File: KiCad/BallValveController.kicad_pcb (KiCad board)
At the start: 2 copper layers, 55.6 x 43.2 mm, 62 parts, among them J1 Screw_Terminal_01x03, J2 Screw_Terminal_01x04, J3 Screw_Terminal_01x04, J4 Screw_Terminal_01x04, J5 Conn_01x01_Male, J6 Screw_Terminal_01x04, J7 Screw_Terminal_01x02, K1 G5V-2, Q1 Q_PMOS_GDS, Q2 2N2222A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

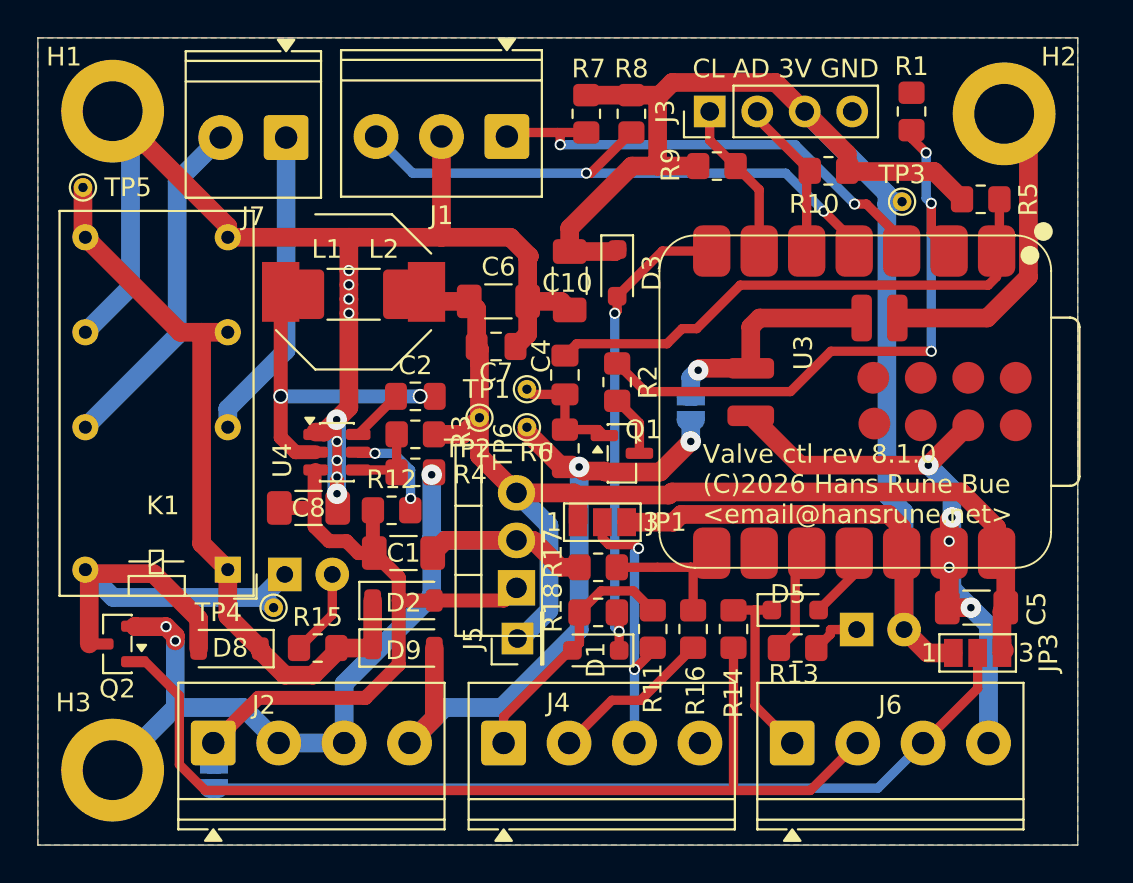
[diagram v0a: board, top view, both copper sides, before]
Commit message: Add ME3116 support via 1x3 pin header
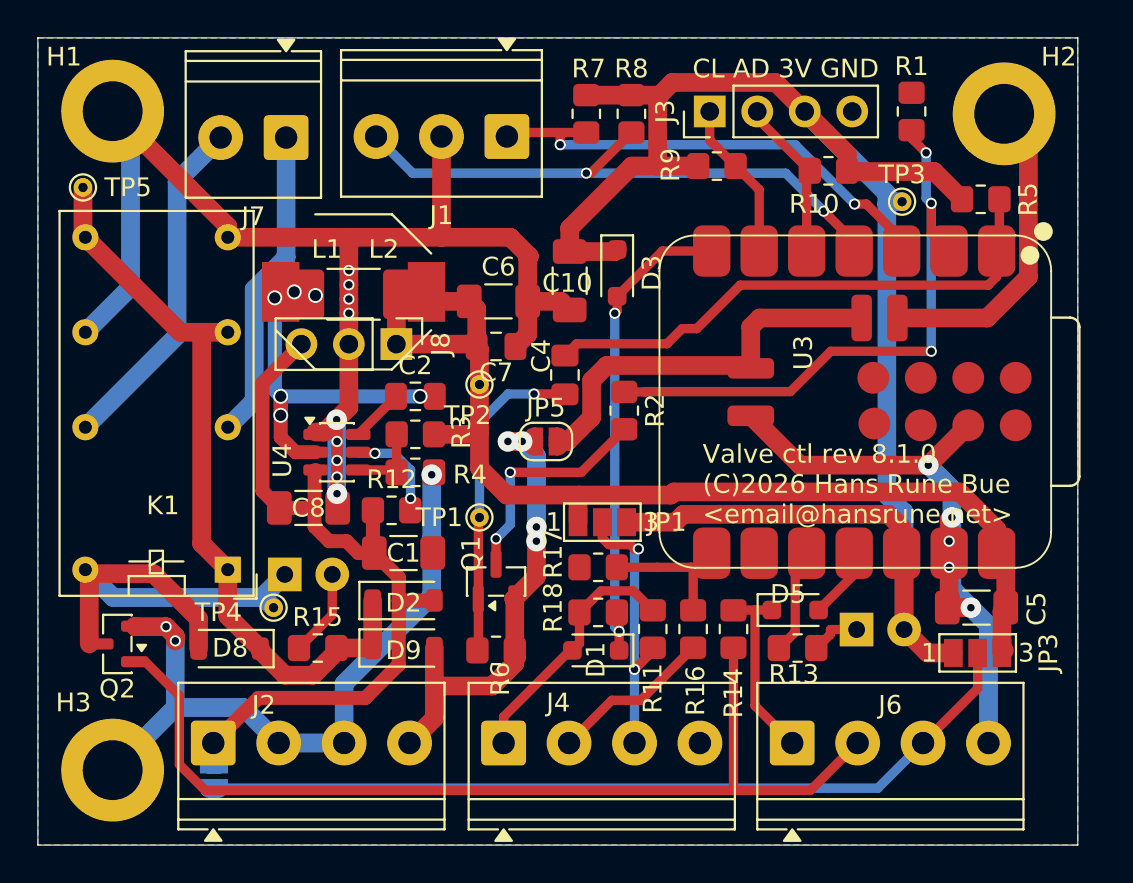
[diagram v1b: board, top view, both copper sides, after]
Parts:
- removed J5: Conn_01x01_Male, Connector_PinHeader_2.54mm:PinHeader_1x01_P2.54mm_Vertical
- removed TP6: TestPoint, TestPoint:TestPoint_THTPad_D1.0mm_Drill0.5mm
- removed U2: L7805, Package_TO_SOT_THT:TO-220-3_Vertical
- added J8: ME3116 in-gnd-out, Connector_PinHeader_2.54mm:PinHeader_1x03_P2.54mm_Vertical, F.Cu at (155.1, 97.5)
- JP5: moved to F.Cu
- moved R6 11.4 mm to (160.4, 113.9), turned to 0 degrees
- moved Q1 9.61 mm to (160.4, 110.2), turned to 90 degrees
- moved JP5 7.95 mm to (163.1, 102.7), turned to 0 degrees
- moved TP1 7.31 mm to (159.5, 106.8)
- moved TP2 1.78 mm to (159.5, 99.7)
- moved R2 1.57 mm to (167.3, 101.1)
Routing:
- net GND: track 175.6 -> 162.4 mm
- net /VBAT: track 37.6 -> 26.4 mm, vias 2 -> 4
- net Net-(Q1-G): track 6.27 -> 17.5 mm, vias 0 -> 1
- net Net-(Q1-D): track 3.30 -> 12.3 mm, vias 0 -> 2
- net /JPBAT: track 12.7 -> 21.6 mm, vias 1 -> 0
- net /PwrIn: track 35.8 -> 41.1 mm
- net /IND1: track 18.2 -> 21.4 mm, vias 2 -> 6
- net +5V: track 61.2 -> 58.9 mm
- net Net-(U3-GPIO1_A1_D1): track 33.5 -> 32.5 mm
